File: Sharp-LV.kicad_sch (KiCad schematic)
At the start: 51 parts, among them J1 USB_C_Receptacle_USB2.0, J2 Conn_01x05_PROG, J3 5024260810, J4 FH52-10S-0.5SH_99, J5 SM04B-SRSS-TB_LF__SN_, J6 Conn_2Rows-13Pins, J7 S2B-PH-SM4-TB_LF__SN_, U1 NRF52840-QIAA-R, U2 USBLC6-2P6, U3 MCP1700-3302E_SOT23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

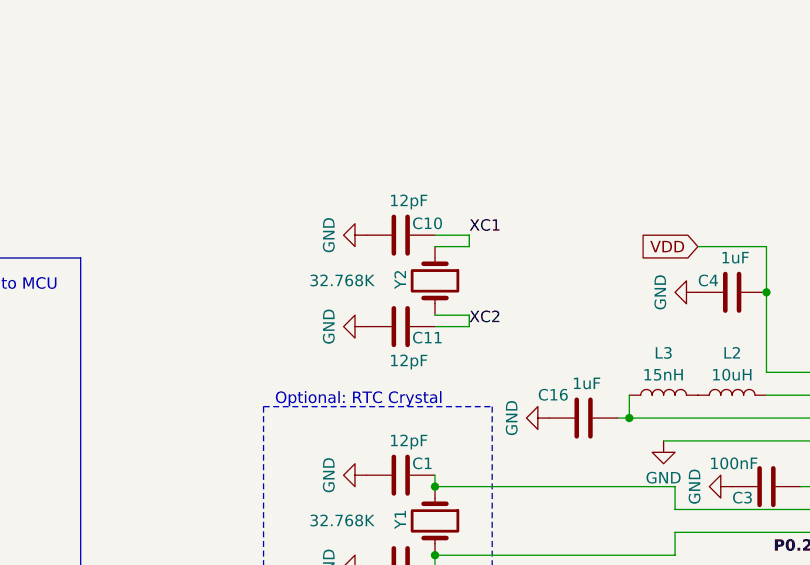
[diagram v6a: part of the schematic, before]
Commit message: Update crystal to the one provided by Mike (32 Mhz)
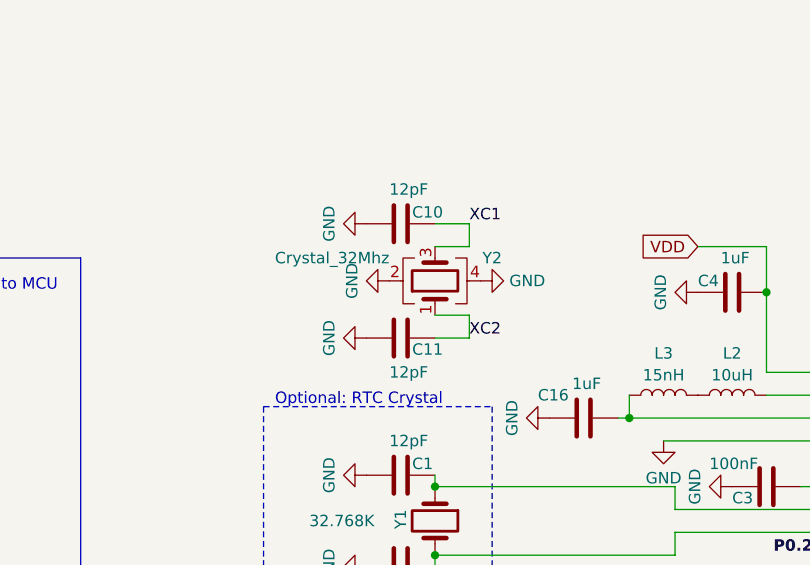
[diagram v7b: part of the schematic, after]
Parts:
- removed Y2: 32.768K, Crystal:Crystal_SMD_3215-2Pin_3.2x1.5mm, symbol Device:Crystal
- added Y2: Crystal_32Mhz, Crystal:Crystal_SMD_2016-4Pin_2.0x1.6mm, symbol Device:Crystal_GND24
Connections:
- net GND: now also Y2.2, Y2.4
- net XC1: now also Y2.3
- net XC2: now also Y2.1
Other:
- moved on the sheet: C10, C11
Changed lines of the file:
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@@
     (stroke (width 0) (type default))
   )
-  (wire (pts (xy 140.97 31.75) (xy 140.97 33.02))
+  (wire (pts (xy 140.97 30.48) (xy 140.97 33.02))
     (stroke (width 0) (type default))
   )
@@
     (stroke (width 0) (type default))
   )
-  (wire (pts (xy 140.97 31.75) (xy 137.16 31.75))
+  (wire (pts (xy 140.97 30.48) (xy 137.16 30.48))
     (stroke (width 0) (type default))
   )
@@
     (stroke (width 0) (type default))
   )
-  (wire (pts (xy 140.97 40.64) (xy 140.97 41.91))
+  (wire (pts (xy 140.97 40.64) (xy 140.97 43.18))
     (stroke (width 0) (type default))
   )
@@
     (stroke (width 0) (type default))
   )
-  (wire (pts (xy 140.97 41.91) (xy 137.16 41.91))
+  (wire (pts (xy 140.97 43.18) (xy 137.16 43.18))
     (stroke (width 0) (type default))
   )
@@
     (effects (font (size 1.27 1.27) (thickness 0.254) bold (color 255 153 0 1)) (justify right bottom))
   )
-  (label "XC1" (at 140.97 31.75 0) (fields_autoplaced)
+  (label "XC1" (at 140.97 30.48 0) (fields_autoplaced)
     (effects (font (size 1.27 1.27)) (justify left bottom))
   )
@@
     (effects (font (size 1.27 1.27) (thickness 0.254) bold (color 255 0 255 1)) (justify right bottom))
   )
-  (label "XC2" (at 140.97 41.91 0) (fields_autoplaced)
+  (label "XC2" (at 140.97 43.18 0) (fields_autoplaced)
     (effects (font (size 1.27 1.27)) (justify left bottom))
   )
@@
     )
   )
-  (symbol (lib_id "power:GND") (at 129.54 31.75 270) (unit 1)
+  (symbol (lib_id "power:GND") (at 129.54 30.48 270) (unit 1)
     (in_bom yes) (on_board yes) (dnp no) (fields_autoplaced)
-    (property "Reference" "#PWR015" (at 123.19 31.75 0)
+    (property "Reference" "#PWR015" (at 123.19 30.48 0)
       (effects (font (size 1.27 1.27)) hide)
     )
-    (property "Value" "GND" (at 125.4069 31.75 0)
+    (property "Value" "GND" (at 125.4069 30.48 0)
       (effects (font (size 1.27 1.27)))
     )
-    (property "Footprint" "" (at 129.54 31.75 0)
+    (property "Footprint" "" (at 129.54 30.48 0)
       (effects (font (size 1.27 1.27)) hide)
     )
-    (property "Datasheet" "" (at 129.54 31.75 0)
+    (property "Datasheet" "" (at 129.54 30.48 0)
       (effects (font (size 1.27 1.27)) hide)
     )
@@
     )
   )
-  (symbol (lib_id "Device:Crystal") (at 137.16 36.83 270) (unit 1)
-    (in_bom yes) (on_board yes) (dnp no)
-    (property "Reference" "Y2" (at 133.35 35.56 0)
-      (effects (font (size 1.27 1.27)) (justify left))
-    )
-    (property "Value" "32.768K" (at 123.19 36.83 90)
-      (effects (font (size 1.27 1.27)) (justify left))
-    )
-    (property "Footprint" "Crystal:Crystal_SMD_3215-2Pin_3.2x1.5mm" (at 137.16 36.83 0)
-      (effects (font (size 1.27 1.27)) hide)
-    )
-    (property "Datasheet" "~" (at 137.16 36.83 0)
-      (effects (font (size 1.27 1.27)) hide)
-    )
-    (property "LCSC" "C32346" (at 137.16 36.83 90)
-      (effects (font (size 1.27 1.27)) hide)
-    )
-    (pin "1")
-    (pin "2")
-    (instances
-      (project "Sharp-LV"
-        (path "/19808d61-e19c-42f1-b3f4-29e10270d8fb"
-          (reference "Y2") (unit 1)
-        )
-      )
-    )
-  )
   (symbol (lib_id "power:GND") (at 364.49 190.5 0) (unit 1)
     (in_bom yes) (on_board yes) (dnp no)
@@
     )
   )
-  (symbol (lib_id "Device:C") (at 133.35 41.91 90) (unit 1)
+  (symbol (lib_id "Device:C") (at 133.35 43.18 90) (unit 1)
     (in_bom yes) (on_board yes) (dnp no)
-    (property "Reference" "C11" (at 134.62 43.18 90)
+    (property "Reference" "C11" (at 134.62 44.45 90)
       (effects (font (size 1.27 1.27)) (justify right))
     )
-    (property "Value" "12pF" (at 132.08 45.72 90)
+    (property "Value" "12pF" (at 132.08 46.99 90)
       (effects (font (size 1.27 1.27)) (justify right))
     )
-    (property "Footprint" "Capacitor_SMD:C_0402_1005Metric" (at 137.16 40.9448 0)
+    (property "Footprint" "Capacitor_SMD:C_0402_1005Metric" (at 137.16 42.2148 0)
       (effects (font (size 1.27 1.27)) hide)
     )
-    (property "Datasheet" "~" (at 133.35 41.91 0)
+    (property "Datasheet" "~" (at 133.35 43.18 0)
       (effects (font (size 1.27 1.27)) hide)
     )
-    (property "LCSC" "C386126" (at 133.35 41.91 0)
+    (property "LCSC" "C386126" (at 133.35 43.18 0)
       (effects (font (size 1.27 1.27)) hide)
     )
@@
     )
   )
-  (symbol (lib_id "power:GND") (at 129.54 41.91 270) (unit 1)
+  (symbol (lib_id "power:GND") (at 129.54 43.18 270) (unit 1)
     (in_bom yes) (on_board yes) (dnp no) (fields_autoplaced)
-    (property "Reference" "#PWR016" (at 123.19 41.91 0)
+    (property "Reference" "#PWR016" (at 123.19 43.18 0)
       (effects (font (size 1.27 1.27)) hide)
     )
-    (property "Value" "GND" (at 125.4069 41.91 0)
+    (property "Value" "GND" (at 125.4069 43.18 0)
       (effects (font (size 1.27 1.27)))
     )
-    (property "Footprint" "" (at 129.54 41.91 0)
+    (property "Footprint" "" (at 129.54 43.18 0)
       (effects (font (size 1.27 1.27)) hide)
     )
-    (property "Datasheet" "" (at 129.54 41.91 0)
+    (property "Datasheet" "" (at 129.54 43.18 0)
       (effects (font (size 1.27 1.27)) hide)
     )
@@
     )
   )
+  (symbol (lib_id "power:GND") (at 132.08 36.83 270) (unit 1)
+    (in_bom yes) (on_board yes) (dnp no) (fields_autoplaced)
+    (property "Reference" "#PWR040" (at 125.73 36.83 0)
+      (effects (font (size 1.27 1.27)) hide)
+    )
+    (property "Value" "GND" (at 127.9469 36.83 0)
+      (effects (font (size 1.27 1.27)))
+    )
+    (property "Footprint" "" (at 132.08 36.83 0)
+      (effects (font (size 1.27 1.27)) hide)
+    )
+    (property "Datasheet" "" (at 132.08 36.83 0)
+      (effects (font (size 1.27 1.27)) hide)
+    )
+    (pin "1")
+    (instances
+      (project "Sharp-LV"
+        (path "/19808d61-e19c-42f1-b3f4-29e10270d8fb"
+          (reference "#PWR040") (unit 1)
+        )
+      )
+    )
+  )
   (symbol (lib_id "power:GND") (at 269.24 106.68 90) (unit 1)
     (in_bom yes) (on_board yes) (dnp no) (fields_autoplaced)
@@
     )
   )
+  (symbol (lib_id "power:GND") (at 142.24 36.83 90) (unit 1)
+    (in_bom yes) (on_board yes) (dnp no) (fields_autoplaced)
+    (property "Reference" "#PWR041" (at 148.59 36.83 0)
+      (effects (font (size 1.27 1.27)) hide)
+    )
+    (property "Value" "GND" (at 145.415 36.83 90)
+      (effects (font (size 1.27 1.27)) (justify right))
+    )
+    (property "Footprint" "" (at 142.24 36.83 0)
+      (effects (font (size 1.27 1.27)) hide)
+    )
+    (property "Datasheet" "" (at 142.24 36.83 0)
+      (effects (font (size 1.27 1.27)) hide)
+    )
+    (pin "1")
+    (instances
+      (project "Sharp-LV"
+        (path "/19808d61-e19c-42f1-b3f4-29e10270d8fb"
+          (reference "#PWR041") (unit 1)
+        )
+      )
+    )
+  )
   (symbol (lib_id "Device:R") (at 85.09 54.61 0) (mirror y) (unit 1)
     (in_bom yes) (on_board yes) (dnp no)
@@
     )
   )
-  (symbol (lib_id "Device:C") (at 133.35 31.75 90) (unit 1)
+  (symbol (lib_id "Device:Crystal_GND24") (at 137.16 36.83 90) (unit 1)
+    (in_bom yes) (on_board yes) (dnp no)
+    (property "Reference" "Y2" (at 143.51 34.29 90)
+      (effects (font (size 1.27 1.27)))
+    )
+    (property "Value" "Crystal_32Mhz" (at 125.73 34.29 90)
+      (effects (font (size 1.27 1.27)))
+    )
+    (property "Footprint" "Crystal:Crystal_SMD_2016-4Pin_2.0x1.6mm" (at 137.16 36.83 0)
+      (effects (font (size 1.27 1.27)) hide)
+    )
+    (property "Datasheet" "~" (at 137.16 36.83 0)
+      (effects (font (size 1.27 1.27)) hide)
+    )
+    (property "LCSC" "C409316" (at 137.16 36.83 90)
+      (effects (font (size 1.27 1.27)) hide)
+    )
+    (pin "3")
+    (pin "1")
+    (pin "2")
+    (pin "4")
+    (instances
+      (project "Sharp-LV"
+        (path "/19808d61-e19c-42f1-b3f4-29e10270d8fb"
+          (reference "Y2") (unit 1)
+        )
+      )
+    )
+  )
+  (symbol (lib_id "Device:C") (at 133.35 30.48 90) (unit 1)
     (in_bom yes) (on_board yes) (dnp no)
-    (property "Reference" "C10" (at 134.62 30.48 90)
+    (property "Reference" "C10" (at 134.62 29.21 90)
       (effects (font (size 1.27 1.27)) (justify right))
     )
-    (property "Value" "12pF" (at 132.08 27.94 90)
+    (property "Value" "12pF" (at 132.08 26.67 90)
       (effects (font (size 1.27 1.27)) (justify right))
     )
-    (property "Footprint" "Capacitor_SMD:C_0402_1005Metric" (at 137.16 30.7848 0)
+    (property "Footprint" "Capacitor_SMD:C_0402_1005Metric" (at 137.16 29.5148 0)
       (effects (font (size 1.27 1.27)) hide)
     )
-    (property "Datasheet" "~" (at 133.35 31.75 0)
+    (property "Datasheet" "~" (at 133.35 30.48 0)
       (effects (font (size 1.27 1.27)) hide)
     )
-    (property "LCSC" "C386126" (at 133.35 31.75 0)
+    (property "LCSC" "C386126" (at 133.35 30.48 0)
       (effects (font (size 1.27 1.27)) hide)
     )

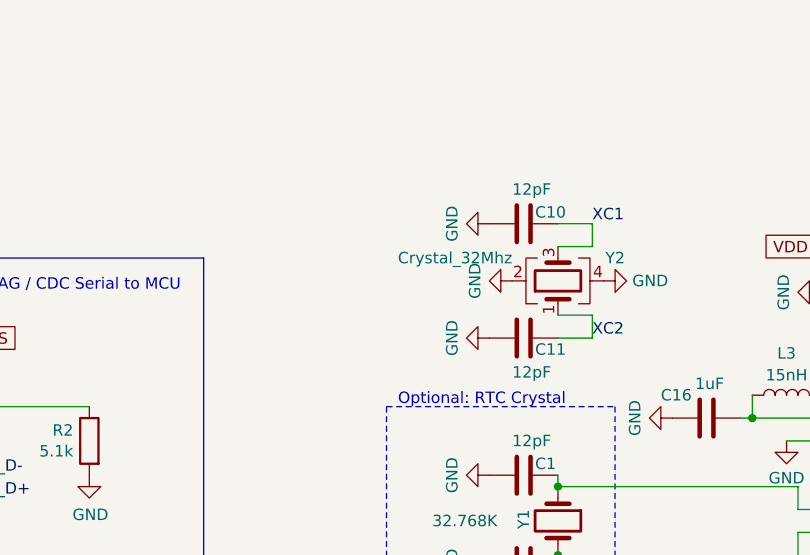
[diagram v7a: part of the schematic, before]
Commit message: update schematic
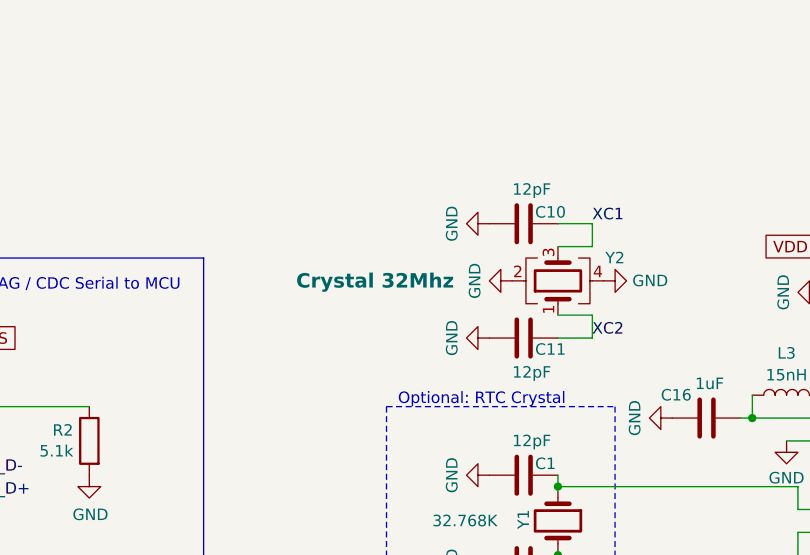
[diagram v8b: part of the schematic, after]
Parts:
- Y2: value Crystal_32Mhz -> Crystal 32Mhz
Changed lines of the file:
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@@
       (effects (font (size 1.27 1.27)))
     )
-    (property "Value" "Crystal_32Mhz" (at 125.73 34.29 90)
-      (effects (font (size 1.27 1.27)))
+    (property "Value" "Crystal 32Mhz" (at 116.84 36.83 90)
+      (effects (font (size 1.6 1.6) bold))
     )
     (property "Footprint" "Crystal:Crystal_SMD_2016-4Pin_2.0x1.6mm" (at 137.16 36.83 0)
